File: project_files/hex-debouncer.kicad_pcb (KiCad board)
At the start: 2 copper layers, 63.5 x 25.4 mm, 45 parts, among them J1 UPPER, SW1 A, SW10 B, SW11 D, SW12 F, SW2 B, SW3 C, SW4 D, SW5 E, SW6 F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

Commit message: Image editing
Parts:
- moved REF** 0.38 mm to (92.1, 63.5)
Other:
- board text added: "Hex Push-Buttons module with Hardware Debouncer"
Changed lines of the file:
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@@
 	(footprint "Symbol:OSHW-Logo_11.4x12mm_SilkScreen"
 		(layer "B.Cu")
-		(at 92.456 63.5 -90)
+		(at 92.075 63.5 -90)
 		(descr "Open Source Hardware Logo")
 		(tags "Logo OSHW")
@@
 		)
 	)
+	(gr_text "Hex Push-Buttons\nmodule with\nHardware Debouncer"
+		(at 69.85 63.5 90)
+		(layer "B.SilkS")
+		(effects
+			(font
+				(size 1.27 1.27)
+				(thickness 0.1905)
+			)
+			(justify mirror)
+		)
+	)
 	(gr_text "C"
 		(at 83.82 53.594 90)
@@
 		)
 	)
+	(gr_text "E"
+		(at 110.49 63.5 0)
+		(layer "F.SilkS")
+		(effects
+			(font
+				(size 2.54 2.54)
+				(thickness 0.508)
+				(bold yes)
+			)
+		)
+	)
+	(gr_text "C"
+		(at 54.61 68.58 0)
+		(layer "F.SilkS")
+		(effects
+			(font
+				(size 2.54 2.54)
+				(thickness 0.508)
+				(bold yes)
+			)
+		)
+	)
+	(gr_text "F"
+		(at 110.49 68.58 0)
+		(layer "F.SilkS")
+		(effects
+			(font
+				(size 2.54 2.54)
+				(thickness 0.508)
+				(bold yes)
+			)
+		)
+	)
 	(gr_text "A"
 		(at 78.74 53.848 0)
@@
 	)
 	(gr_text "D"
+		(at 110.49 58.42 0)
+		(layer "F.SilkS")
+		(effects
+			(font
+				(size 2.54 2.54)
+				(thickness 0.508)
+				(bold yes)
+			)
+		)
+	)
+	(gr_text "D"
 		(at 86.36 53.848 0)
 		(layer "F.SilkS" knockout)
@@
 				(size 1.016 1.016)
 				(thickness 0.1905)
+				(bold yes)
+			)
+		)
+	)
+	(gr_text "B"
+		(at 54.61 63.5 0)
+		(layer "F.SilkS")
+		(effects
+			(font
+				(size 2.54 2.54)
+				(thickness 0.508)
 				(bold yes)
 			)
@@
 				(bold yes)
 			)
+		)
+	)
+	(gr_text "A"
+		(at 54.61 58.42 0)
+		(layer "F.SilkS")
+		(effects
+			(font
+				(size 2.54 2.54)
+				(thickness 0.508)
+				(bold yes)
+			)

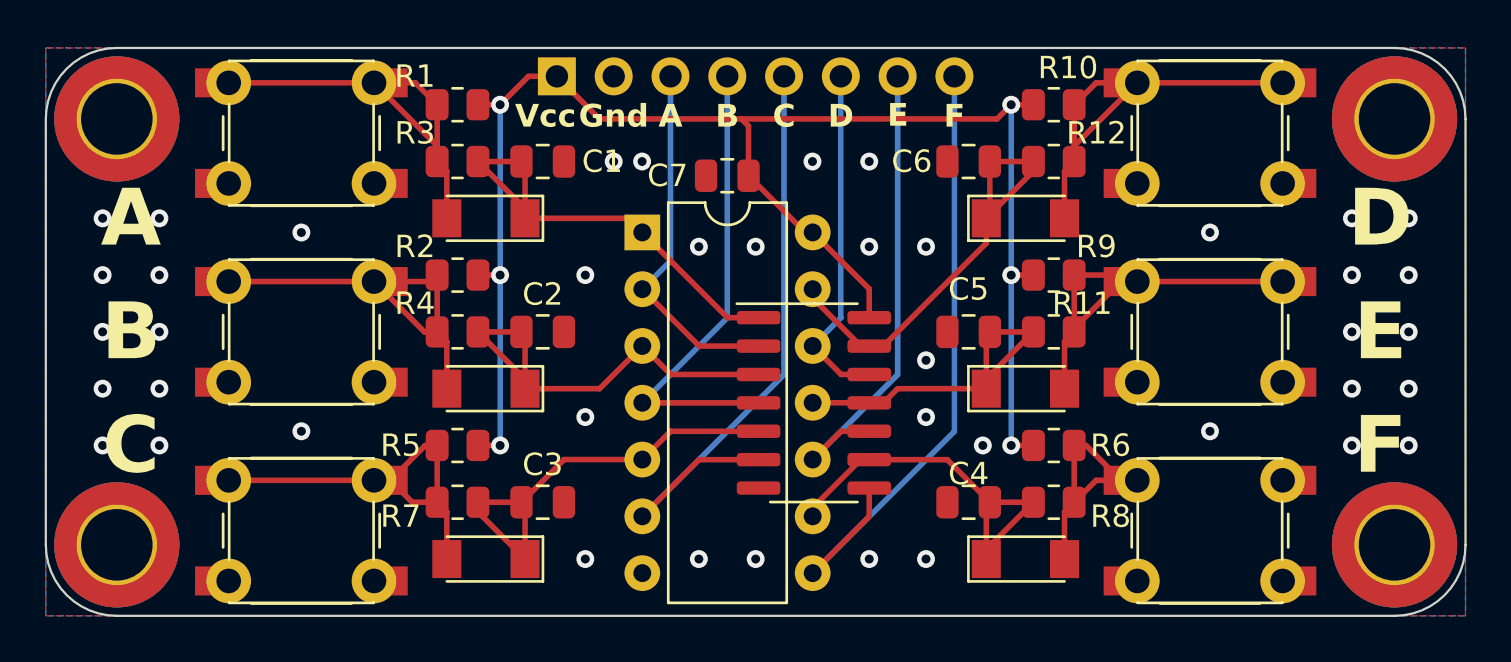
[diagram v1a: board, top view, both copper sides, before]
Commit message: rerouted with 0.5 mm tracks
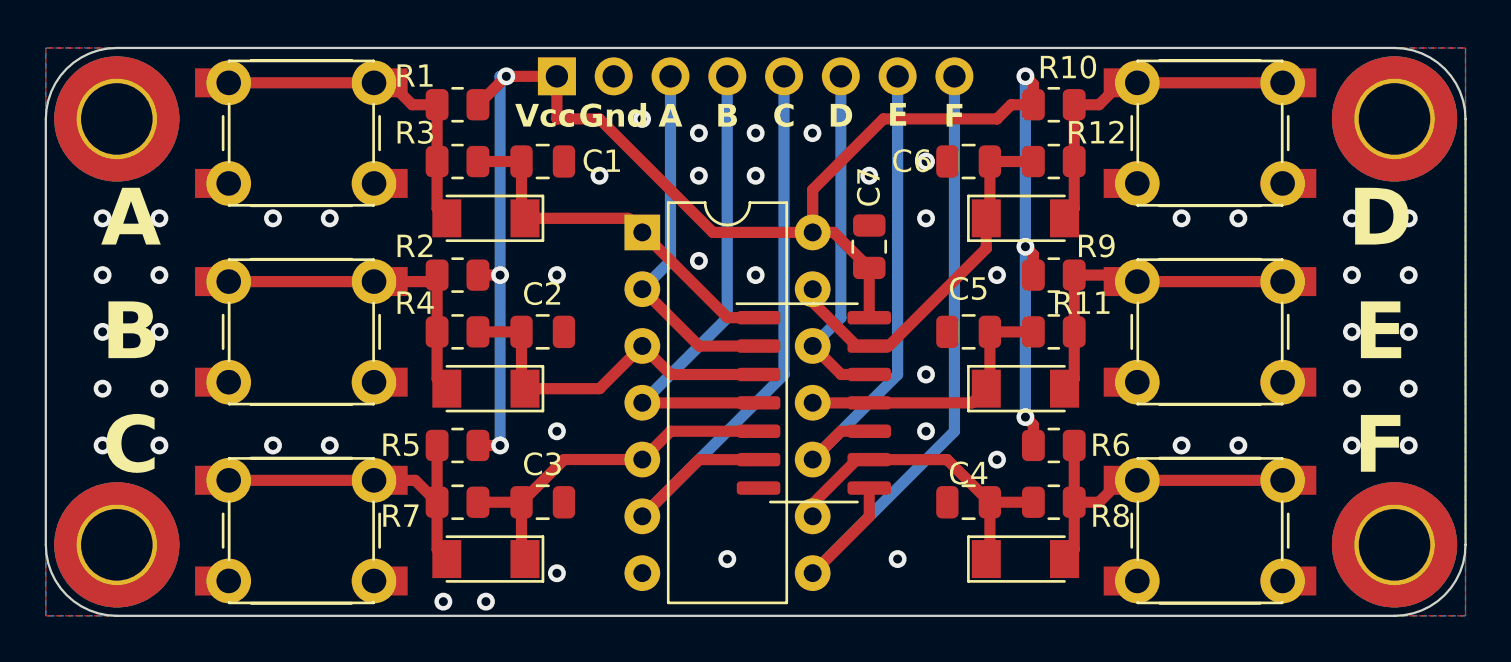
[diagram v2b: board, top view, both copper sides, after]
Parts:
- moved C7 7.10 mm to (87.6, 59.7), turned to 90 degrees
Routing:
- net Net-(D6-A): track 18.9 -> 14.3 mm
- net Net-(D1-A): track 18.9 -> 14.3 mm
- net VCC: track 72.3 -> 76.9 mm
- net Net-(D2-A): track 18.5 -> 14.0 mm
- net Net-(D4-A): track 10.5 -> 14.3 mm
- net /BUT_E: track 16.0 -> 12.6 mm
- net /BUT_B: track 19.7 -> 16.3 mm
- net /BUT_A: track 20.3 -> 16.8 mm
- net /BUT_C: track 19.9 -> 16.5 mm
- net /BUT_F: track 18.0 -> 14.6 mm
- net /BUT_D: track 20.0 -> 16.9 mm
- net Net-(D5-A): track 17.1 -> 14.0 mm
- net Net-(D3-A): track 17.0 -> 14.3 mm
- net GND: vias 42 -> 51
